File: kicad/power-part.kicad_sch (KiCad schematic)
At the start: 52 parts, among them Q10 BSS84, Q11 BSS123N, Q12 ZXMP10A17GTA, Q2 IPT015N10N5, Q3 IPT015N10N5, Q4 IPT015N10N5, Q5 IPT015N10N5, Q6 IPT015N10N5, Q7 IPT015N10N5, Q8 IPT015N10N5, Q9 IPT015N10N5

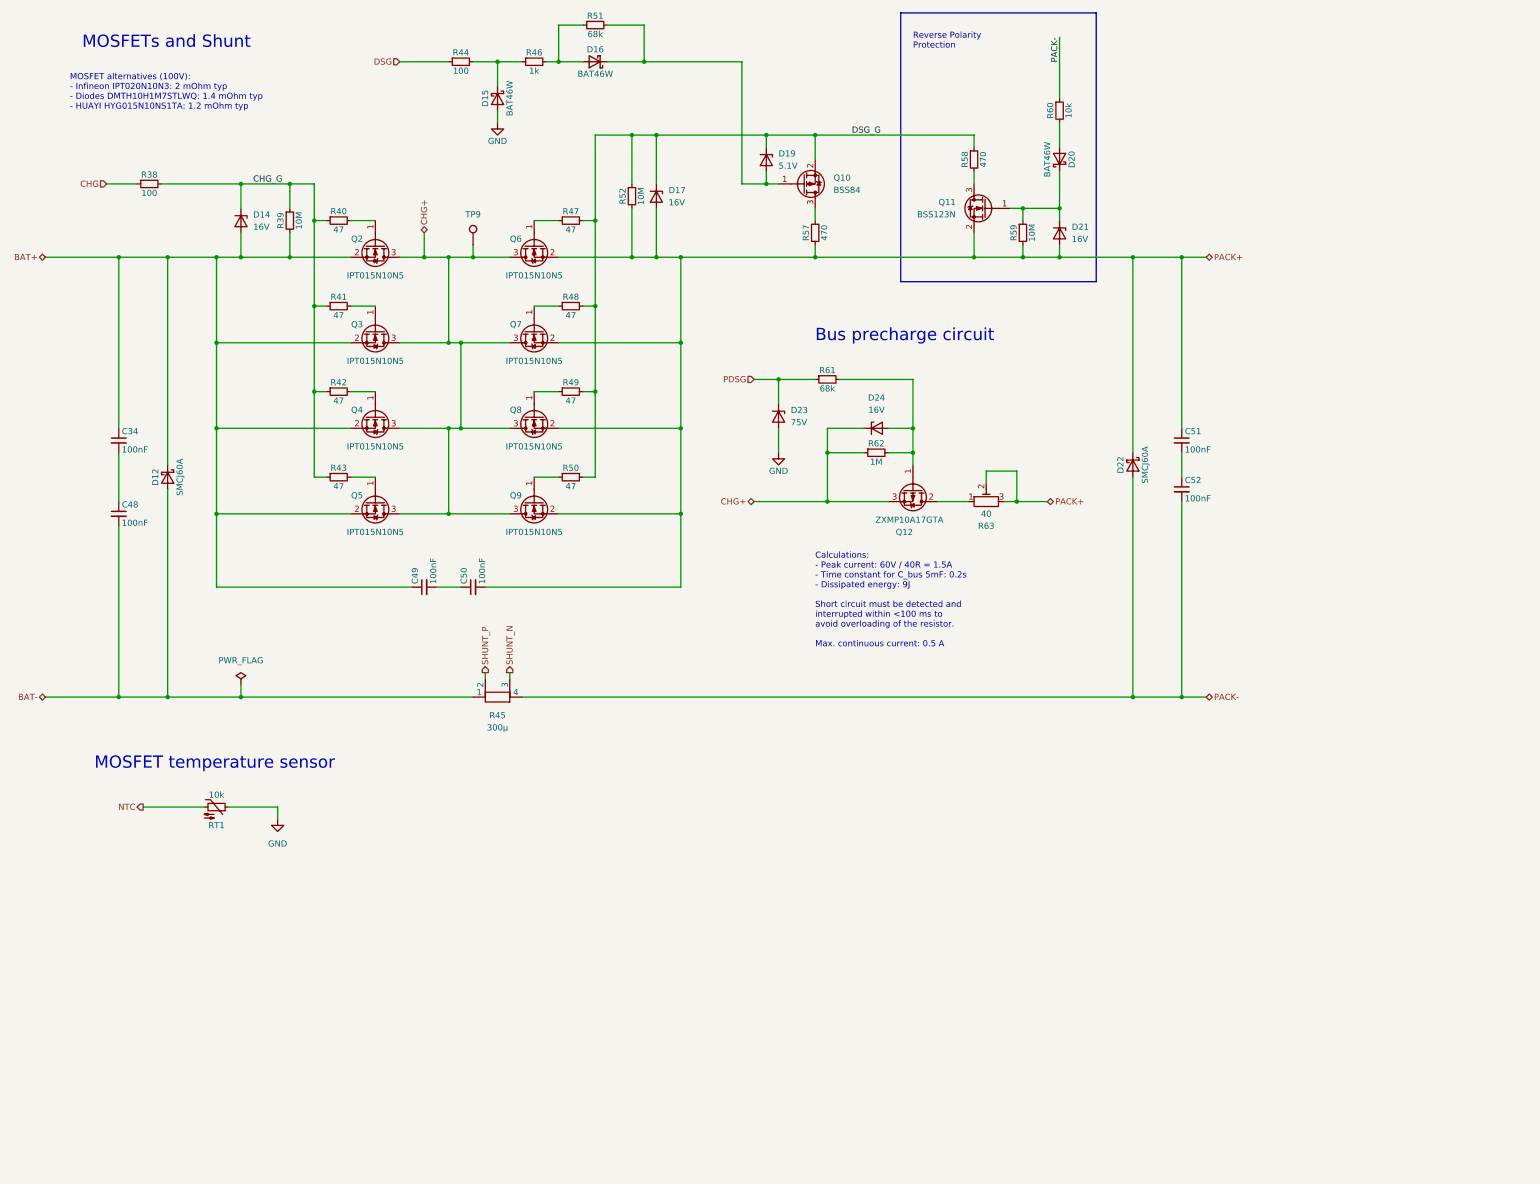
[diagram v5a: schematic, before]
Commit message: v0.4.0: Multiple improvements for new board revision
- Use LMR38010 for internal power supply (max. 80V instead of 60V)
- Change USB connector from Micro-A to C and remove 5V power supply
  which was not working anyway. The board cannot be powered by USB
  only.
- Add TS2 (connected to DFETOFF) to measure shunt temperature
- Add RS-485 transceiver (sharing the connector with CAN)
- Switch I2C pins of ESP32-C3 to GPIO8/9. This allows to re-use the
  I2C pull-ups for strapping configuration and frees two pins for the
  RS-485 transceiver RE and DE pins. Also we may get rid of the I2C
  glitches during start-up.
- Use 80V instead of 100V power MOSFETs to reduce Rds(on).
- Reduce DSG gate resistor R57 to 47R to increase switch-off speed.
- Adjust some resistors to reduce number of different parts
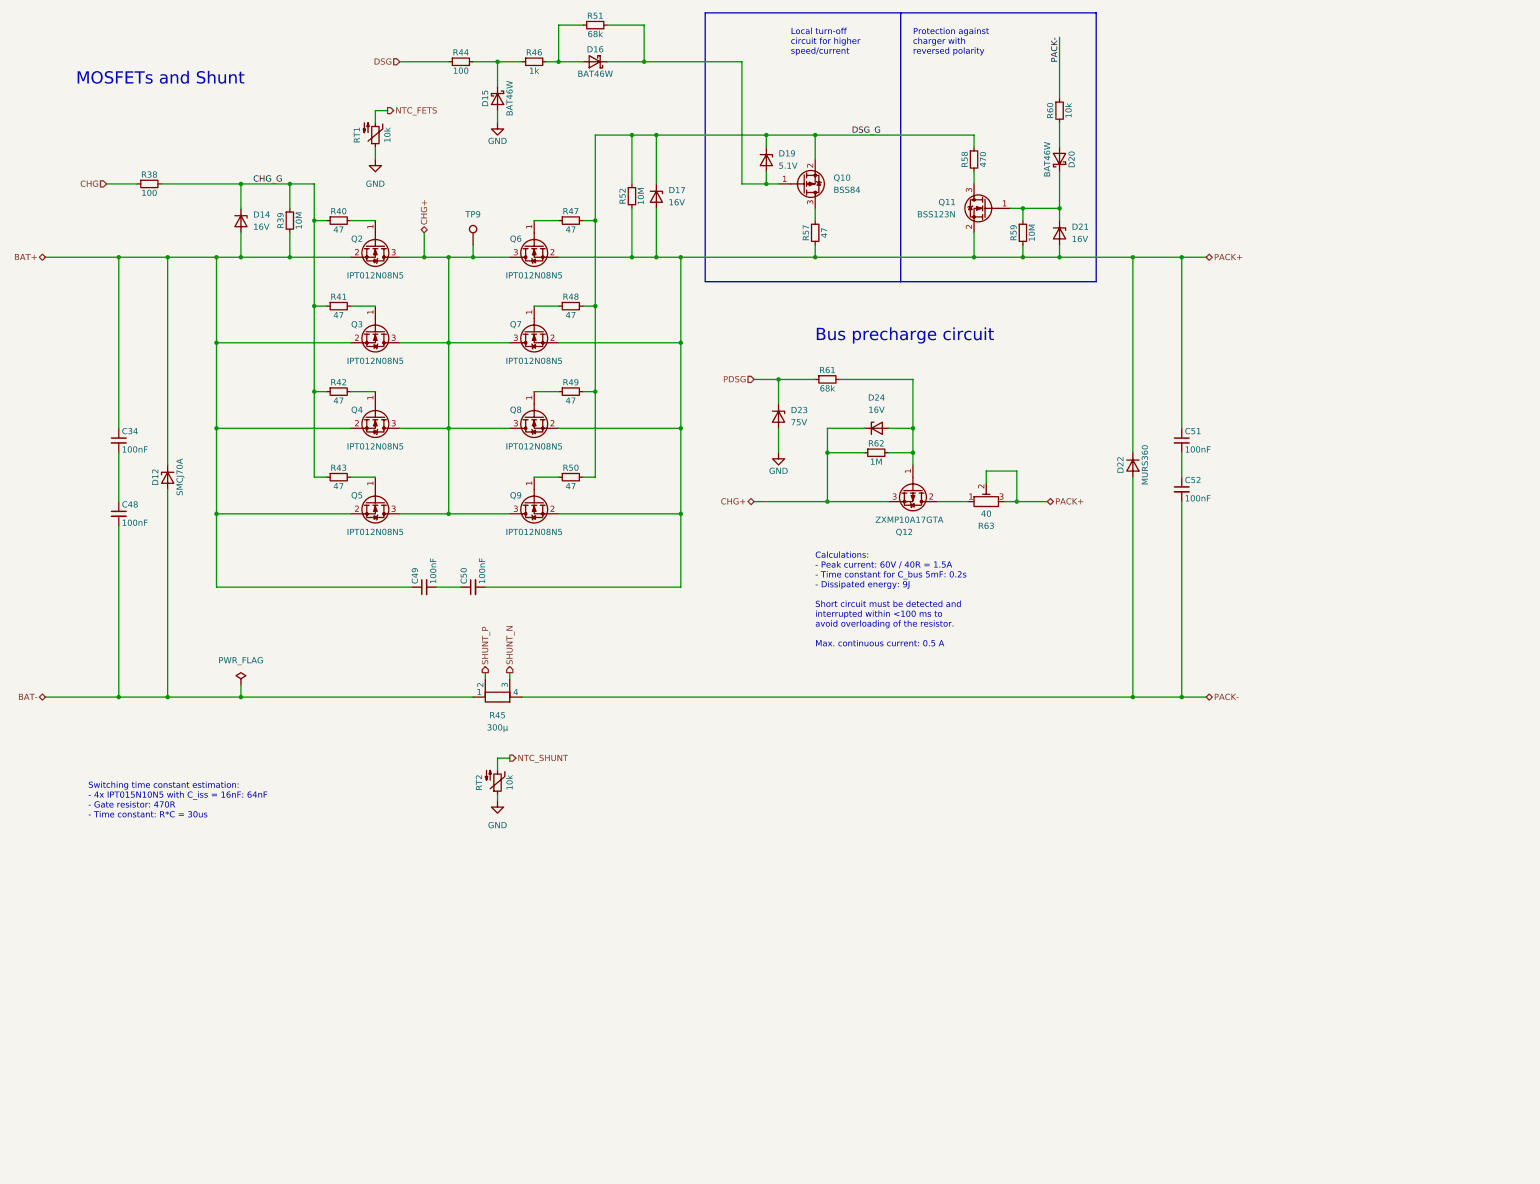
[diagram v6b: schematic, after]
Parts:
- added RT2: 10k, LibreSolar:R_0603_1608, symbol LibreSolar:R_NTC
- C34, C48, C49, C50, C51, C52: LCSC (none) -> C15725; Manufacturer any -> Samsung Electro-Mechanics; PartNumber (none) -> CL10B104KC8NNNC; Remarks X7R, 100V -> min. 100V, X7R
- D12: value SMCJ60A -> SMCJ70A; symbol LibreSolar:D_Schottky -> LibreSolar:D_Zener; LCSC (none) -> C135194; PartNumber SMCJ60A -> SMCJ70A; Remarks Alternative: Diodes Inc. SMCJ60A-13-F -> Alternative: Diodes Inc. SMCJ70A-13-F
- D14, D17, D21, D24: LCSC (none) -> C282317
- D15, D16, D20: LCSC (none) -> C83152
- D19: LCSC (none) -> C151348
- D22: value SMCJ60A -> MURS360; symbol LibreSolar:D_Schottky -> LibreSolar:D; LCSC (none) -> C388245; Manufacturer Bourns -> Diodes Incorporated; PartNumber SMCJ60A -> MURS360; Remarks Alternative: Diodes Inc. SMCJ60A-13-F -> Alternative: Other MURS360
- D23: LCSC (none) -> C266795
- Q10: LCSC (none) -> C127273
- Q11: LCSC (none) -> C534594; Manufacturer any -> Infineon; PartNumber BSS123N -> BSS123N H6327
- Q12: LCSC (none) -> C32998
- Q2, Q3, Q4, Q5, Q6, Q7, Q8, Q9: value IPT015N10N5 -> IPT012N08N5; LCSC (none) -> C531199; PartNumber IPT015N10N5 -> IPT012N08N5; Remarks Alternative with 2mOhm: IPT020N10N3 -> Alternative: Huayi HYG012N08NS1TA
- R38, R44: Manufacturer any -> Yageo; PartNumber (none) -> RC0603FR-07100RL
- R39, R52, R59: Manufacturer any -> Yageo; PartNumber (none) -> RC0603FR-0710ML
- R40, R41, R42, R43, R47, R48, R49, R50: Manufacturer any -> Yageo; PartNumber (none) -> RC0603FR-0747RL
- R46: Manufacturer any -> Yageo; PartNumber (none) -> RC0603FR-071KL
- R51, R61: Manufacturer any -> Yageo; PartNumber (none) -> RC0603FR-0768KL
- R57: value 470 -> 47; Manufacturer any -> Yageo; PartNumber (none) -> RC0603FR-0747RL
- R58: Manufacturer any -> Yageo; PartNumber (none) -> RC0603FR-07470RL
- R60: Manufacturer any -> Yageo; PartNumber (none) -> RC0603FR-0710KL
- R62: Manufacturer any -> Yageo; PartNumber (none) -> RC0603FR-071ML
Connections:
- net GND: now also RT2.1
- net NTC renamed NTC_FETS
- new net NTC_SHUNT: RT2.2
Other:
- note added: "Local turn-off circuit for higher speed/current"
- note added: "Protection against charger with reversed polarity"
- note added: "Switching time constant estimation: - 4x IPT015N10N5 with C_iss = 16nF: 64nF - Gate resistor: 470R - Time constant: R*C = 30us"
- note removed: "MOSFET alternatives (100V): - Infineon IPT020N10N3: 2 mOhm typ - Diodes DMTH10H1M7STLWQ: 1.4 mOhm typ - HUAYI HYG015N10NS1TA: 1.2 mOhm typ"
- note removed: "MOSFET temperature sensor"
- note removed: "Reverse Polarity Protection"
- moved on the sheet: RT1

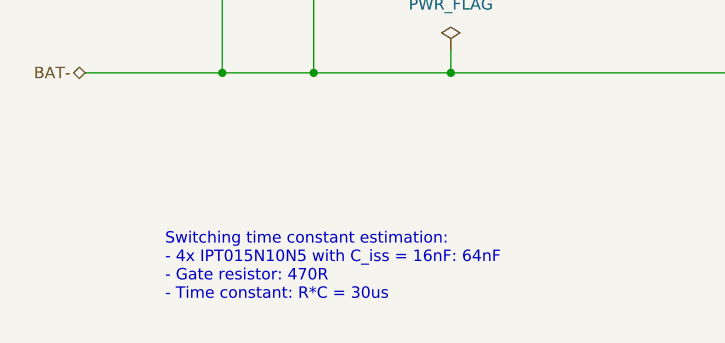
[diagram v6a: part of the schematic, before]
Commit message: Fix schematic page numbers and MOSFET time constant calc
Fixes #49
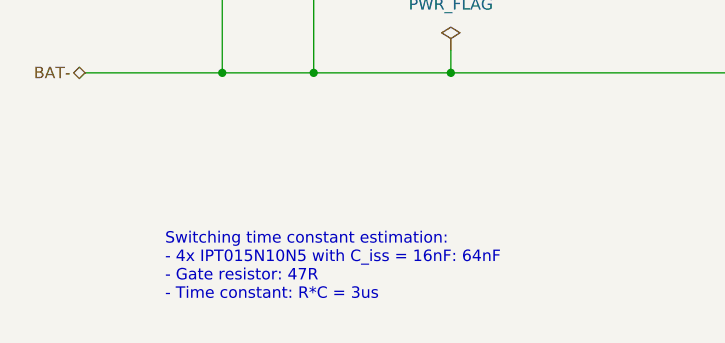
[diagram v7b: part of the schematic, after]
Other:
- note added: "Switching time constant estimation: - 4x IPT015N10N5 with C_iss = 16nF: 64nF - Gate resistor: 47R - Time constant: R*C = 3us"
- note removed: "Switching time constant estimation: - 4x IPT015N10N5 with C_iss = 16nF: 64nF - Gate resistor: 470R - Time constant: R*C = 30us"
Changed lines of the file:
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@@
     (effects (font (size 1.27 1.27)) (justify left bottom))
   )
-  (text "Switching time constant estimation:\n- 4x IPT015N10N5 with C_iss = 16nF: 64nF\n- Gate resistor: 470R\n- Time constant: R*C = 30us"
+  (text "Switching time constant estimation:\n- 4x IPT015N10N5 with C_iss = 16nF: 64nF\n- Gate resistor: 47R\n- Time constant: R*C = 3us"
     (at 36.83 185.42 0)
     (effects (font (size 1.27 1.27)) (justify left bottom))

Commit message: fix: Field Remarks of component Q2-Q8 contains extra spaces
kibot throws following warnings:
WARNING:(W037) Field Remarks of component Q5 (Q_NMOS_GSD IPT012N08N5) contains extra spaces: `Alternative: Huayi HYG012N08NS1TA ` removing them. (kibot - v5_sch.py:1057)
WARNING:(W037) Field Remarks of component Q3 (Q_NMOS_GSD IPT012N08N5) contains extra spaces: `Alternative: Huayi HYG012N08NS1TA ` removing them. (kibot - v5_sch.py:1057)
WARNING:(W037) Field Remarks of component Q4 (Q_NMOS_GSD IPT012N08N5) contains extra spaces: `Alternative: Huayi HYG012N08NS1TA ` removing them. (kibot - v5_sch.py:1057)
WARNING:(W037) Field Remarks of component Q9 (Q_NMOS_GSD IPT012N08N5) contains extra spaces: `Alternative: Huayi HYG012N08NS1TA ` removing them. (kibot - v5_sch.py:1057)
WARNING:(W037) Field Remarks of component Q2 (Q_NMOS_GSD IPT012N08N5) contains extra spaces: `Alternative: Huayi HYG012N08NS1TA ` removing them. (kibot - v5_sch.py:1057)
WARNING:(W037) Field Remarks of component Q6 (Q_NMOS_GSD IPT012N08N5) contains extra spaces: `Alternative: Huayi HYG012N08NS1TA ` removing them. (kibot - v5_sch.py:1057)
WARNING:(W037) Field Remarks of component Q8 (Q_NMOS_GSD IPT012N08N5) contains extra spaces: `Alternative: Huayi HYG012N08NS1TA ` removing them. (kibot - v5_sch.py:1057)
WARNING:(W037) Field Remarks of component Q7 (Q_NMOS_GSD IPT012N08N5) contains extra spaces: `Alternative: Huayi HYG012N08NS1TA ` removing them. (kibot - v5_sch.py:1057)
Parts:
- Q2, Q3, Q4, Q5, Q6, Q7, Q8, Q9: Remarks Alternative: Huayi HYG012N08NS1TA -> Alternative: Huayi HYG012N08NS1TA
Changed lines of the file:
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@@
       (effects (font (size 1.27 1.27)) hide)
     )
-    (property "Remarks" "Alternative: Huayi HYG012N08NS1TA " (at 96.52 119.38 0)
+    (property "Remarks" "Alternative: Huayi HYG012N08NS1TA" (at 96.52 119.38 0)
       (effects (font (size 1.27 1.27)) hide)
     )
@@
       (effects (font (size 1.27 1.27)) hide)
     )
-    (property "Remarks" "Alternative: Huayi HYG012N08NS1TA " (at 96.52 83.82 0)
+    (property "Remarks" "Alternative: Huayi HYG012N08NS1TA" (at 96.52 83.82 0)
       (effects (font (size 1.27 1.27)) hide)
     )
@@
       (effects (font (size 1.27 1.27)) hide)
     )
-    (property "Remarks" "Alternative: Huayi HYG012N08NS1TA " (at 96.52 101.6 0)
+    (property "Remarks" "Alternative: Huayi HYG012N08NS1TA" (at 96.52 101.6 0)
       (effects (font (size 1.27 1.27)) hide)
     )
@@
       (effects (font (size 1.27 1.27)) hide)
     )
-    (property "Remarks" "Alternative: Huayi HYG012N08NS1TA " (at 129.54 119.38 0)
+    (property "Remarks" "Alternative: Huayi HYG012N08NS1TA" (at 129.54 119.38 0)
       (effects (font (size 1.27 1.27)) hide)
     )
@@
       (effects (font (size 1.27 1.27)) hide)
     )
-    (property "Remarks" "Alternative: Huayi HYG012N08NS1TA " (at 96.52 66.04 0)
+    (property "Remarks" "Alternative: Huayi HYG012N08NS1TA" (at 96.52 66.04 0)
       (effects (font (size 1.27 1.27)) hide)
     )
@@
       (effects (font (size 1.27 1.27)) hide)
     )
-    (property "Remarks" "Alternative: Huayi HYG012N08NS1TA " (at 129.54 66.04 0)
+    (property "Remarks" "Alternative: Huayi HYG012N08NS1TA" (at 129.54 66.04 0)
       (effects (font (size 1.27 1.27)) hide)
     )
@@
       (effects (font (size 1.27 1.27)) hide)
     )
-    (property "Remarks" "Alternative: Huayi HYG012N08NS1TA " (at 129.54 101.6 0)
+    (property "Remarks" "Alternative: Huayi HYG012N08NS1TA" (at 129.54 101.6 0)
       (effects (font (size 1.27 1.27)) hide)
     )
@@
       (effects (font (size 1.27 1.27)) hide)
     )
-    (property "Remarks" "Alternative: Huayi HYG012N08NS1TA " (at 129.54 83.82 0)
-      (effects (font (size 1.27 1.27)) hide)
-    )
+    (property "Remarks" "Alternative: Huayi HYG012N08NS1TA" (at 129.54 83.82 0)
+      (effects (font (size 1.27 1.27)) hide)
+    )
